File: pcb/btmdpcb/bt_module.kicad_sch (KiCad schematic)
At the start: 21 parts, among them J2 ANT, T1 ED8_4, T2 ED8_4

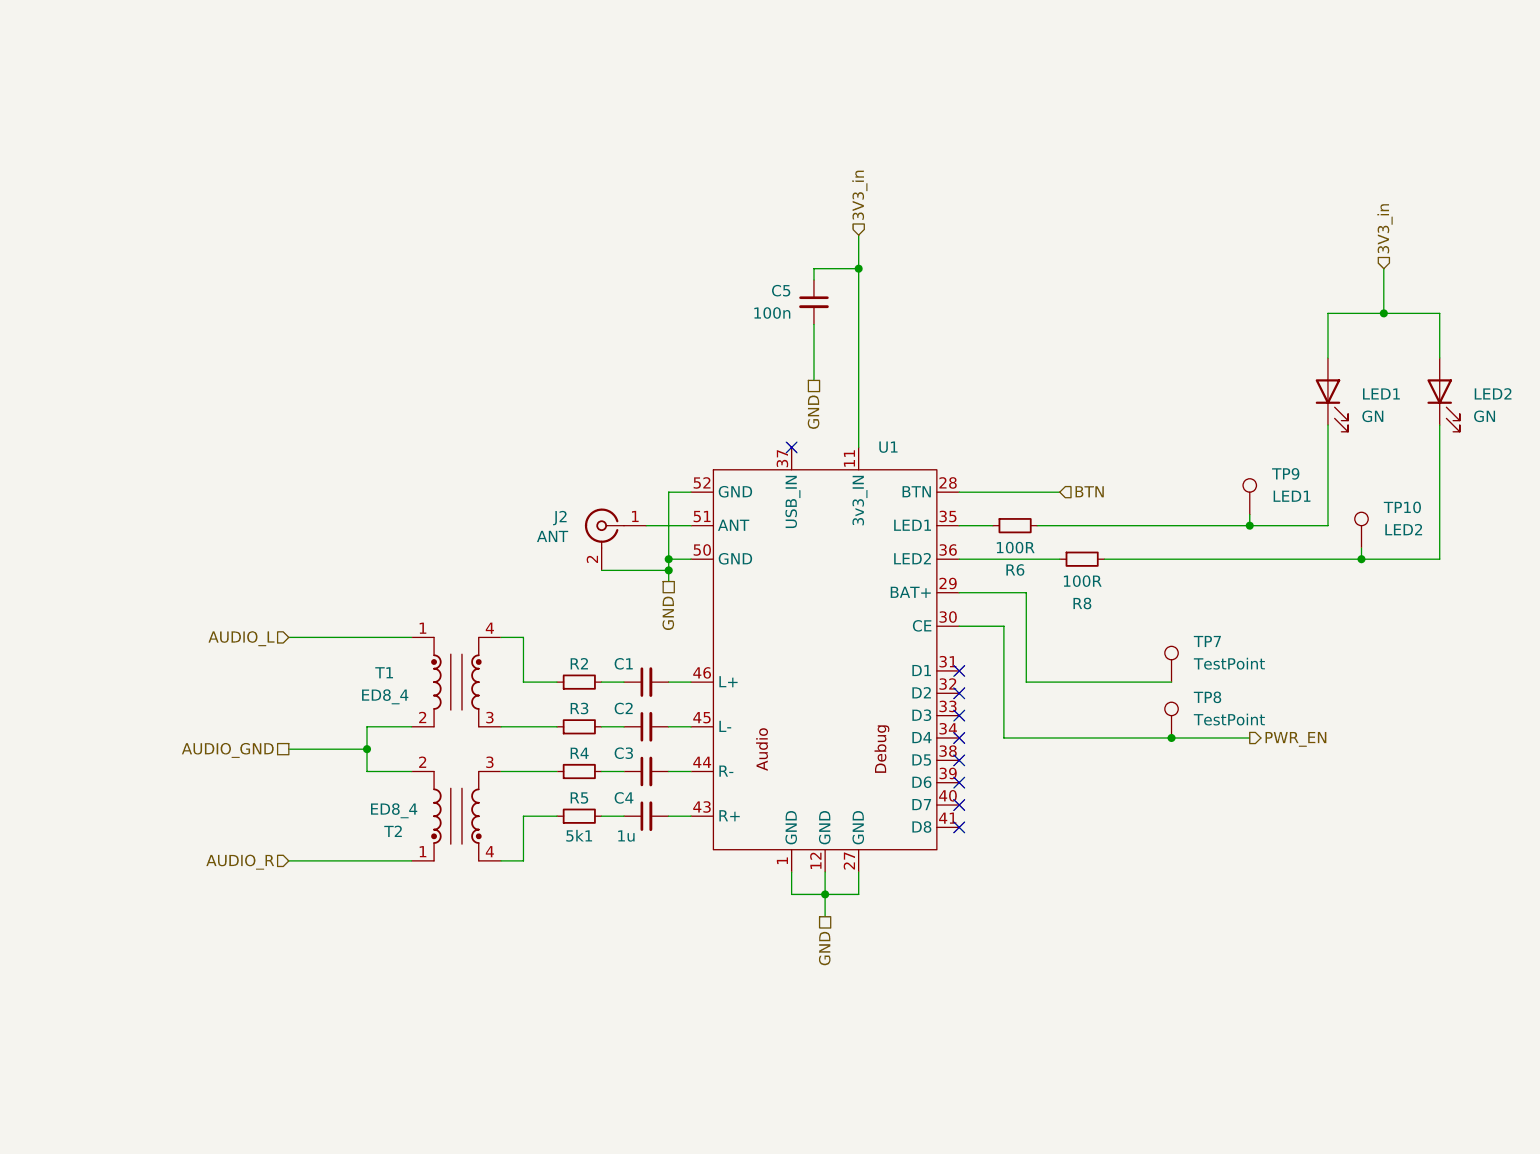
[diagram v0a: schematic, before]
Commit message: Clean up schematic, implement all logic functionality
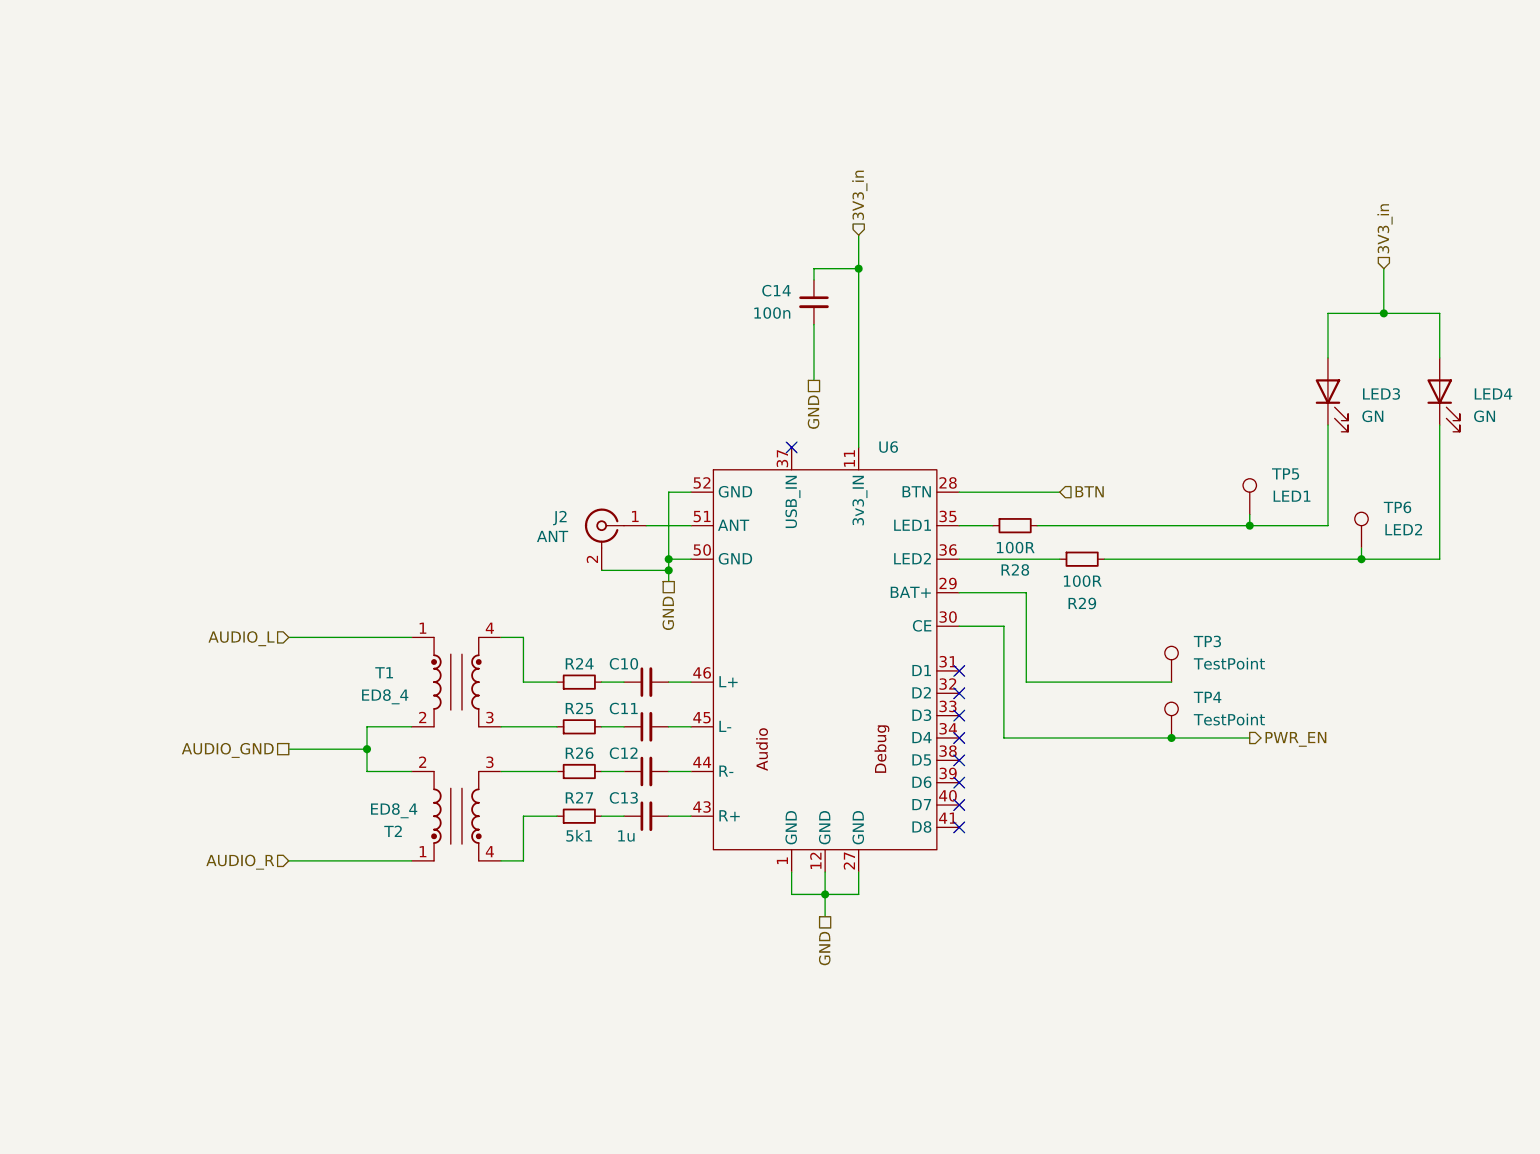
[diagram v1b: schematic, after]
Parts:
- renumbered C1 to C10, C2 to C11, C3 to C12, C4 to C13, C5 to C14, LED1 to LED3, LED2 to LED4, R2 to R24, R3 to R25, R4 to R26, R5 to R27, R6 to R28, R8 to R29, TP7 to TP3, TP8 to TP4, TP9 to TP5, TP10 to TP6, U1 to U6
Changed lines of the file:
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@@
 		(on_board yes)
 		(dnp no)
-		(property "Reference" "R2"
+		(property "Reference" "R24"
 			(at 111.76 99.568 90)
 			(effects
@@
 			(project "btmdpcb"
 				(path "/6e43e92f-e106-411c-86ee-217d084aee5b/5e29ed5f-7cd2-4605-9d5a-4da2465d4bbc"
-					(reference "R2")
+					(reference "R24")
 					(unit 1)
 				)
@@
 		(dnp no)
 		(fields_autoplaced yes)
-		(property "Reference" "TP7"
+		(property "Reference" "TP3"
 			(at 181.61 97.0279 0)
 			(effects
@@
 			(project "btmdpcb"
 				(path "/6e43e92f-e106-411c-86ee-217d084aee5b/5e29ed5f-7cd2-4605-9d5a-4da2465d4bbc"
-					(reference "TP7")
+					(reference "TP3")
 					(unit 1)
 				)
@@
 		(on_board yes)
 		(dnp no)
-		(property "Reference" "R6"
+		(property "Reference" "R28"
 			(at 161.29 88.9 90)
 			(effects
@@
 			(project "btmdpcb"
 				(path "/6e43e92f-e106-411c-86ee-217d084aee5b/5e29ed5f-7cd2-4605-9d5a-4da2465d4bbc"
-					(reference "R6")
+					(reference "R28")
 					(unit 1)
 				)
@@
 		(on_board yes)
 		(dnp no)
-		(property "Reference" "C2"
+		(property "Reference" "C11"
 			(at 116.84 104.648 90)
 			(effects
@@
 			(project "btmdpcb"
 				(path "/6e43e92f-e106-411c-86ee-217d084aee5b/5e29ed5f-7cd2-4605-9d5a-4da2465d4bbc"
-					(reference "C2")
+					(reference "C11")
 					(unit 1)
 				)
@@
 		(on_board yes)
 		(dnp no)
-		(property "Reference" "TP9"
+		(property "Reference" "TP5"
 			(at 190.5 77.9779 0)
 			(effects
@@
 			(project "btmdpcb"
 				(path "/6e43e92f-e106-411c-86ee-217d084aee5b/5e29ed5f-7cd2-4605-9d5a-4da2465d4bbc"
-					(reference "TP9")
+					(reference "TP5")
 					(unit 1)
 				)
@@
 		(on_board yes)
 		(dnp no)
-		(property "Reference" "R5"
+		(property "Reference" "R27"
 			(at 111.76 114.808 90)
 			(effects
@@
 			(project "btmdpcb"
 				(path "/6e43e92f-e106-411c-86ee-217d084aee5b/5e29ed5f-7cd2-4605-9d5a-4da2465d4bbc"
-					(reference "R5")
+					(reference "R27")
 					(unit 1)
 				)
@@
 		(on_board yes)
 		(dnp no)
-		(property "Reference" "R8"
+		(property "Reference" "R29"
 			(at 168.91 92.71 90)
 			(effects
@@
 			(project "btmdpcb"
 				(path "/6e43e92f-e106-411c-86ee-217d084aee5b/5e29ed5f-7cd2-4605-9d5a-4da2465d4bbc"
-					(reference "R8")
+					(reference "R29")
 					(unit 1)
 				)
@@
 		(on_board yes)
 		(dnp no)
-		(property "Reference" "R3"
+		(property "Reference" "R25"
 			(at 111.76 104.648 90)
 			(effects
@@
 			(project "btmdpcb"
 				(path "/6e43e92f-e106-411c-86ee-217d084aee5b/5e29ed5f-7cd2-4605-9d5a-4da2465d4bbc"
-					(reference "R3")
+					(reference "R25")
 					(unit 1)
 				)
@@
 		(dnp no)
 		(fields_autoplaced yes)
-		(property "Reference" "TP8"
+		(property "Reference" "TP4"
 			(at 181.61 103.3779 0)
 			(effects
@@
 			(project "btmdpcb"
 				(path "/6e43e92f-e106-411c-86ee-217d084aee5b/5e29ed5f-7cd2-4605-9d5a-4da2465d4bbc"
-					(reference "TP8")
+					(reference "TP4")
 					(unit 1)
 				)
@@
 		(dnp no)
 		(fields_autoplaced yes)
-		(property "Reference" "LED2"
+		(property "Reference" "LED4"
 			(at 213.36 68.8974 90)
 			(effects
@@
 			(project "btmdpcb"
 				(path "/6e43e92f-e106-411c-86ee-217d084aee5b/5e29ed5f-7cd2-4605-9d5a-4da2465d4bbc"
-					(reference "LED2")
+					(reference "LED4")
 					(unit 1)
 				)
@@
 		(on_board yes)
 		(dnp no)
-		(property "Reference" "R4"
+		(property "Reference" "R26"
 			(at 111.76 109.728 90)
 			(effects
@@
 			(project "btmdpcb"
 				(path "/6e43e92f-e106-411c-86ee-217d084aee5b/5e29ed5f-7cd2-4605-9d5a-4da2465d4bbc"
-					(reference "R4")
+					(reference "R26")
 					(unit 1)
 				)
@@
 		(on_board yes)
 		(dnp no)
-		(property "Reference" "C3"
+		(property "Reference" "C12"
 			(at 116.84 109.728 90)
 			(effects
@@
 			(project "btmdpcb"
 				(path "/6e43e92f-e106-411c-86ee-217d084aee5b/5e29ed5f-7cd2-4605-9d5a-4da2465d4bbc"
-					(reference "C3")
+					(reference "C12")
 					(unit 1)
 				)
@@
 		(on_board yes)
 		(dnp no)
-		(property "Reference" "C1"
+		(property "Reference" "C10"
 			(at 116.84 99.568 90)
 			(effects
@@
 			(project "btmdpcb"
 				(path "/6e43e92f-e106-411c-86ee-217d084aee5b/5e29ed5f-7cd2-4605-9d5a-4da2465d4bbc"
-					(reference "C1")
+					(reference "C10")
 					(unit 1)
 				)
@@
 		(on_board yes)
 		(dnp no)
-		(property "Reference" "C5"
+		(property "Reference" "C14"
 			(at 135.89 57.1562 0)
 			(effects
@@
 			(project "btmdpcb"
 				(path "/6e43e92f-e106-411c-86ee-217d084aee5b/5e29ed5f-7cd2-4605-9d5a-4da2465d4bbc"
-					(reference "C5")
+					(reference "C14")
 					(unit 1)
 				)
@@
 		(on_board yes)
 		(dnp no)
-		(property "Reference" "C4"
+		(property "Reference" "C13"
 			(at 116.84 114.808 90)
 			(effects
@@
 			(project "btmdpcb"
 				(path "/6e43e92f-e106-411c-86ee-217d084aee5b/5e29ed5f-7cd2-4605-9d5a-4da2465d4bbc"
-					(reference "C4")
+					(reference "C13")
 					(unit 1)
 				)
@@
 		(on_board yes)
 		(dnp no)
-		(property "Reference" "U1"
+		(property "Reference" "U6"
 			(at 145.7041 74.93 0)
 			(effects
@@
 			(project "btmdpcb"
 				(path "/6e43e92f-e106-411c-86ee-217d084aee5b/5e29ed5f-7cd2-4605-9d5a-4da2465d4bbc"
-					(reference "U1")
+					(reference "U6")
 					(unit 1)
 				)
@@
 		(on_board yes)
 		(dnp no)
-		(property "Reference" "TP10"
+		(property "Reference" "TP6"
 			(at 203.2 81.7879 0)
 			(effects
@@
 			(project "btmdpcb"
 				(path "/6e43e92f-e106-411c-86ee-217d084aee5b/5e29ed5f-7cd2-4605-9d5a-4da2465d4bbc"
-					(reference "TP10")
+					(reference "TP6")
 					(unit 1)
 				)
@@
 		(dnp no)
 		(fields_autoplaced yes)
-		(property "Reference" "LED1"
+		(property "Reference" "LED3"
 			(at 200.66 68.8974 90)
 			(effects
@@
 			(project "btmdpcb"
 				(path "/6e43e92f-e106-411c-86ee-217d084aee5b/5e29ed5f-7cd2-4605-9d5a-4da2465d4bbc"
-					(reference "LED1")
-					(unit 1)
-				)
+					(reference "LED3")
+					(unit 1)
+				)

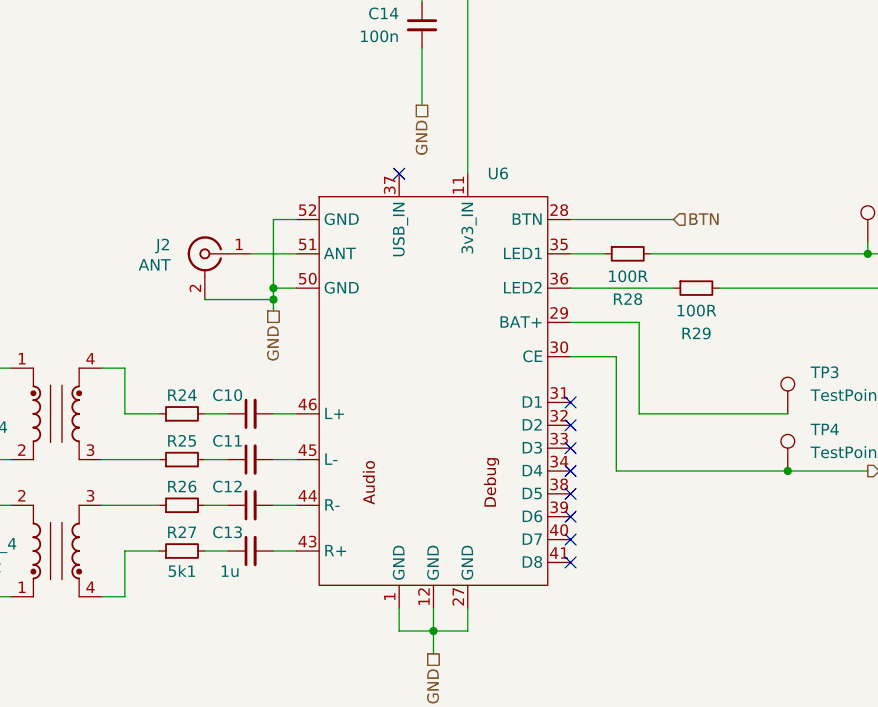
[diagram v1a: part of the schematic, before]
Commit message: Remove redundant regulators, simplify schematic
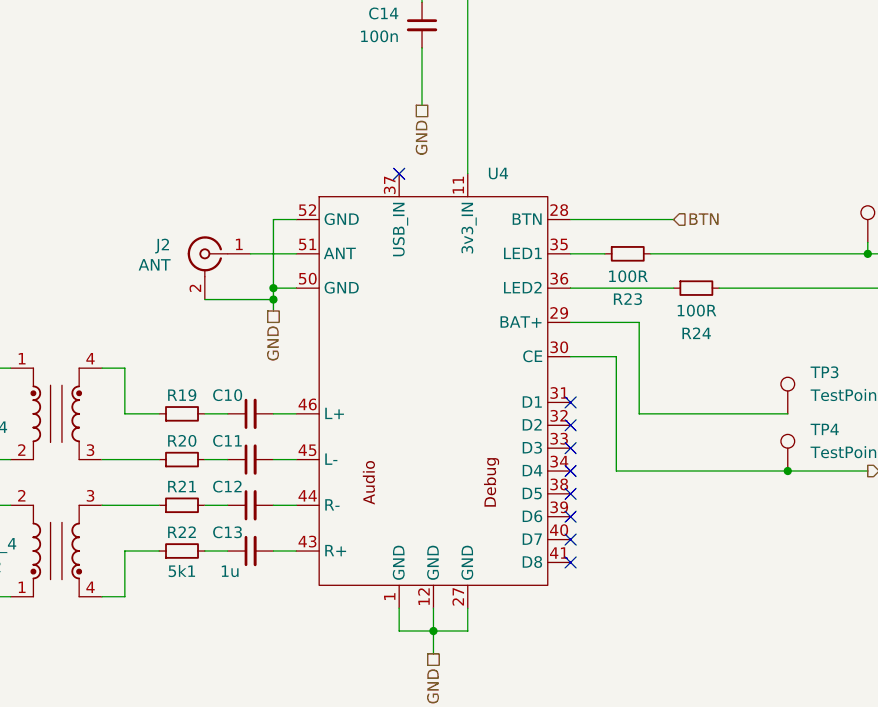
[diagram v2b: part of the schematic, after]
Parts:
- renumbered R24 to R19, R25 to R20, R26 to R21, R27 to R22, R28 to R23, R29 to R24, U6 to U4
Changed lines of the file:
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@@
 		(on_board yes)
 		(dnp no)
-		(property "Reference" "R24"
+		(property "Reference" "R19"
 			(at 111.76 99.568 90)
 			(effects
@@
 			(project "btmdpcb"
 				(path "/6e43e92f-e106-411c-86ee-217d084aee5b/5e29ed5f-7cd2-4605-9d5a-4da2465d4bbc"
-					(reference "R24")
+					(reference "R19")
 					(unit 1)
 				)
@@
 		(on_board yes)
 		(dnp no)
-		(property "Reference" "R28"
+		(property "Reference" "R23"
 			(at 161.29 88.9 90)
 			(effects
@@
 			(project "btmdpcb"
 				(path "/6e43e92f-e106-411c-86ee-217d084aee5b/5e29ed5f-7cd2-4605-9d5a-4da2465d4bbc"
-					(reference "R28")
+					(reference "R23")
 					(unit 1)
 				)
@@
 		(on_board yes)
 		(dnp no)
-		(property "Reference" "R27"
+		(property "Reference" "R22"
 			(at 111.76 114.808 90)
 			(effects
@@
 			(project "btmdpcb"
 				(path "/6e43e92f-e106-411c-86ee-217d084aee5b/5e29ed5f-7cd2-4605-9d5a-4da2465d4bbc"
-					(reference "R27")
+					(reference "R22")
 					(unit 1)
 				)
@@
 		(on_board yes)
 		(dnp no)
-		(property "Reference" "R29"
+		(property "Reference" "R24"
 			(at 168.91 92.71 90)
 			(effects
@@
 			(project "btmdpcb"
 				(path "/6e43e92f-e106-411c-86ee-217d084aee5b/5e29ed5f-7cd2-4605-9d5a-4da2465d4bbc"
-					(reference "R29")
+					(reference "R24")
 					(unit 1)
 				)
@@
 		(on_board yes)
 		(dnp no)
-		(property "Reference" "R25"
+		(property "Reference" "R20"
 			(at 111.76 104.648 90)
 			(effects
@@
 			(project "btmdpcb"
 				(path "/6e43e92f-e106-411c-86ee-217d084aee5b/5e29ed5f-7cd2-4605-9d5a-4da2465d4bbc"
-					(reference "R25")
+					(reference "R20")
 					(unit 1)
 				)
@@
 		(on_board yes)
 		(dnp no)
-		(property "Reference" "R26"
+		(property "Reference" "R21"
 			(at 111.76 109.728 90)
 			(effects
@@
 			(project "btmdpcb"
 				(path "/6e43e92f-e106-411c-86ee-217d084aee5b/5e29ed5f-7cd2-4605-9d5a-4da2465d4bbc"
-					(reference "R26")
+					(reference "R21")
 					(unit 1)
 				)
@@
 		(on_board yes)
 		(dnp no)
-		(property "Reference" "U6"
+		(property "Reference" "U4"
 			(at 145.7041 74.93 0)
 			(effects
@@
 			(project "btmdpcb"
 				(path "/6e43e92f-e106-411c-86ee-217d084aee5b/5e29ed5f-7cd2-4605-9d5a-4da2465d4bbc"
-					(reference "U6")
-					(unit 1)
-				)
+					(reference "U4")
+					(unit 1)
+				)
